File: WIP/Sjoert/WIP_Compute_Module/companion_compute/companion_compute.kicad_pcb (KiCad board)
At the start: 20 copper layers, 34 x 33.8 mm, 71 parts

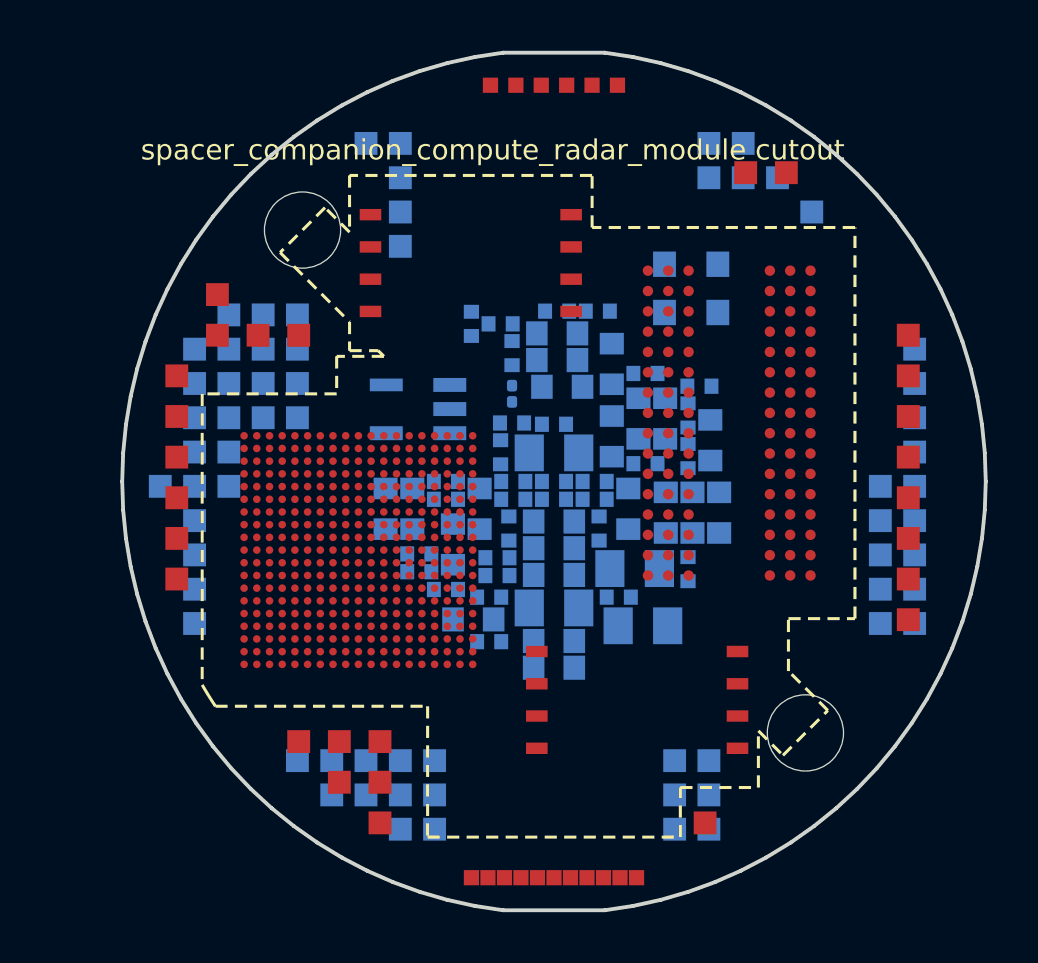
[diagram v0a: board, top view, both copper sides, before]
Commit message: board prepared for stm32mp2 14 layer according to NCAB stackup
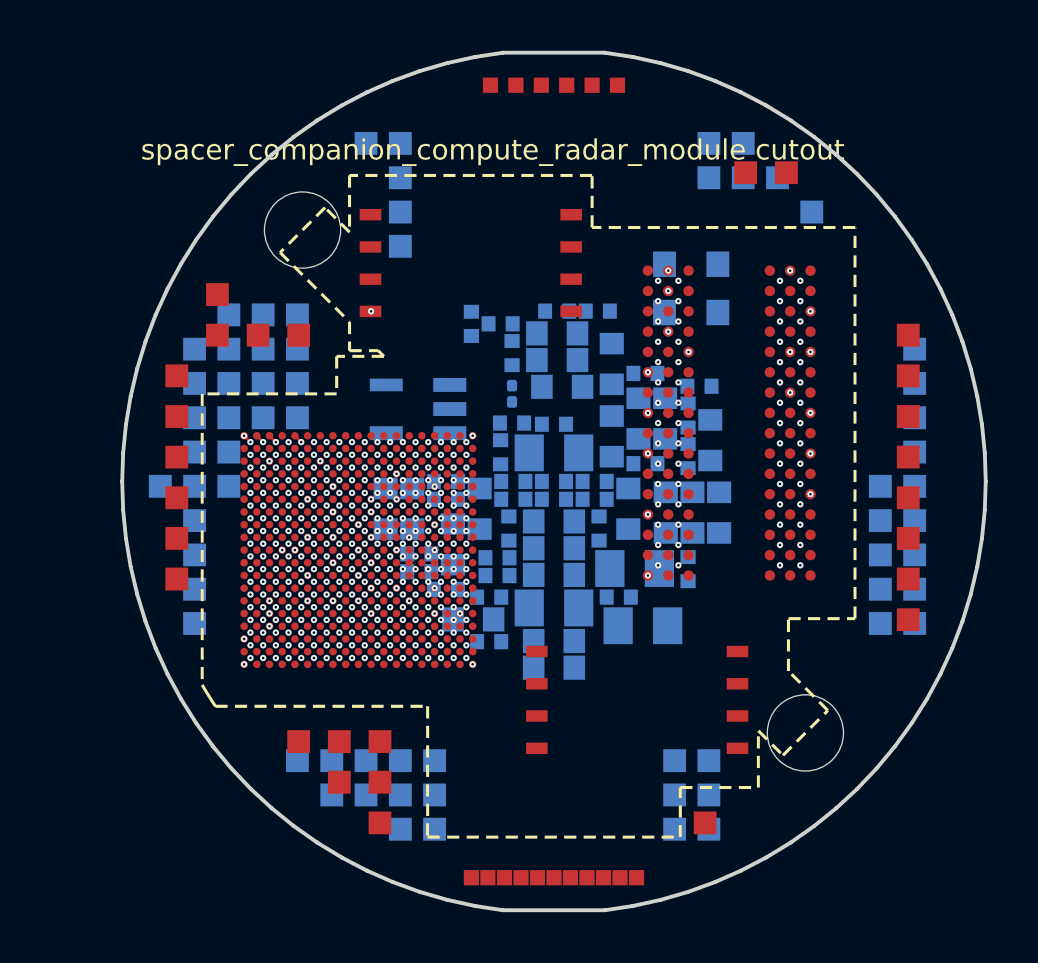
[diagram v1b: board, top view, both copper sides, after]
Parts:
- turned U_MPU to -90 degrees
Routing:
- net FLEX_GND: track 0.00 -> 0.71 mm, vias 0 -> 425
- net SWO: track 0.00 -> 0.35 mm, vias 0 -> 1
- net COMP_HSE_IN: track 0.00 -> 0.35 mm, vias 0 -> 1
- net WBA_UART_RX: vias 0 -> 1
- net TMP1_ALERT: vias 0 -> 1
- net SYS_I2C_SDA: vias 0 -> 1
- net SYS_I2C_SCL: vias 0 -> 1
- net RADAR_EN: vias 0 -> 1
- net NAND_OSPI_IO3: vias 0 -> 1
- net GPIO_EXT_1: vias 0 -> 1
- net DDR4_DQ1: vias 0 -> 1
- net COMP_3V3: vias 0 -> 2
- net COMP_1V8: vias 0 -> 1
- net COMP_0V9: vias 0 -> 2
- net COMP_0V82: vias 0 -> 3
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- added copper zone on In1.Cu, net FLEX_GND
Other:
- copper layers 20 -> 14
- rule pad_to_mask_clearance: 0 -> 0.03
